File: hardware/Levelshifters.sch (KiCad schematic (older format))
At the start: 36 parts, among them U1401 SN74AXC8T245, U1402 SN74AXC8T245, U1403 SN74AXC8T245, U1404 LSF0102, U1405 LSF0102

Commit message: Length matched DDR3 Memory again.
Forgot to keep enough space between the traces and between the meander waves.

Also, I switched to Kicad 5.0 RC2.

Swaped a few ddr signals.
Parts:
- C1401, C1402, C1403, C1404, C1405, C1406, C1407, C1408: symbol C_Small -> device:C_Small
- D1401, D1402: symbol LED_Small -> device:LED_Small
- R1401, R1402, R1403, R1404, R1405, R1406, R1407, R1408, R1409, R1410, R1411, R1412, R1413, R1414, R1415, R1416, R1417, R1418, R1419, R1420, R1421: symbol R_Small -> device:R_Small
- U1401, U1402, U1403: symbol SN74AXC8T245 -> sn74axc8t245:SN74AXC8T245
- U1404, U1405: symbol LSF0102 -> lsf0102:LSF0102

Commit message: Layouted USB-UART.
Also moved USB-OTG to the right Side of the Board. To get there
some free Space, i moved the DDR3/Memory and the FPGA a few
Millimeters down.
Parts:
- R1401, R1402, R1403, R1404, R1405, R1406, R1407, R1408, R1409, R1410, R1411, R1412, R1413, R1414, R1415, R1416, R1417, R1418, R1419, R1420, R1421: footprint Resistors_SMD:R_0402 -> Resistor_SMD:R_0402_1005Metric
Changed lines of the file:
@@
 F 0 "R1407" H 3430 5820 50  0000 L CNN
 F 1 "10k" H 3430 5760 50  0000 L CNN
-F 2 "Resistors_SMD:R_0402" H 3400 5800 50  0001 C CNN
+F 2 "Resistor_SMD:R_0402_1005Metric" H 3400 5800 50  0001 C CNN
 F 3 "" H 3400 5800 50  0001 C CNN
 	1    3400 5800
@@
 F 0 "R1408" H 3430 6820 50  0000 L CNN
 F 1 "10k" H 3430 6760 50  0000 L CNN
-F 2 "Resistors_SMD:R_0402" H 3400 6800 50  0001 C CNN
+F 2 "Resistor_SMD:R_0402_1005Metric" H 3400 6800 50  0001 C CNN
 F 3 "" H 3400 6800 50  0001 C CNN
 	1    3400 6800
@@
 F 0 "R1401" H 3380 1220 50  0000 L CNN
 F 1 "10k" H 3380 1160 50  0000 L CNN
-F 2 "Resistors_SMD:R_0402" H 3350 1200 50  0001 C CNN
+F 2 "Resistor_SMD:R_0402_1005Metric" H 3350 1200 50  0001 C CNN
 F 3 "" H 3350 1200 50  0001 C CNN
 F 4 "1" H 3350 1200 60  0001 C CNN "Populated"
@@
 F 0 "R1404" H 3380 3520 50  0000 L CNN
 F 1 "10k" H 3380 3460 50  0000 L CNN
-F 2 "Resistors_SMD:R_0402" H 3350 3500 50  0001 C CNN
+F 2 "Resistor_SMD:R_0402_1005Metric" H 3350 3500 50  0001 C CNN
 F 3 "" H 3350 3500 50  0001 C CNN
 	1    3350 3500
@@
 F 0 "R1405" H 3380 4520 50  0000 L CNN
 F 1 "10k" H 3380 4460 50  0000 L CNN
-F 2 "Resistors_SMD:R_0402" H 3350 4500 50  0001 C CNN
+F 2 "Resistor_SMD:R_0402_1005Metric" H 3350 4500 50  0001 C CNN
 F 3 "" H 3350 4500 50  0001 C CNN
 	1    3350 4500
@@
 F 0 "R1403" H 3380 2420 50  0000 L CNN
 F 1 "10k" H 3380 2360 50  0000 L CNN
-F 2 "Resistors_SMD:R_0402" H 3350 2400 50  0001 C CNN
+F 2 "Resistor_SMD:R_0402_1005Metric" H 3350 2400 50  0001 C CNN
 F 3 "" H 3350 2400 50  0001 C CNN
 	1    3350 2400
@@
 F 0 "R1406" H 3380 4720 50  0000 L CNN
 F 1 "10k" H 3380 4660 50  0000 L CNN
-F 2 "Resistors_SMD:R_0402" H 3350 4700 50  0001 C CNN
+F 2 "Resistor_SMD:R_0402_1005Metric" H 3350 4700 50  0001 C CNN
 F 3 "" H 3350 4700 50  0001 C CNN
 	1    3350 4700
@@
 F 0 "R1409" H 3430 7020 50  0000 L CNN
 F 1 "10k" H 3430 6960 50  0000 L CNN
-F 2 "Resistors_SMD:R_0402" H 3400 7000 50  0001 C CNN
+F 2 "Resistor_SMD:R_0402_1005Metric" H 3400 7000 50  0001 C CNN
 F 3 "" H 3400 7000 50  0001 C CNN
 	1    3400 7000
@@
 F 0 "R1402" H 3380 2220 50  0000 L CNN
 F 1 "10k" H 3380 2160 50  0000 L CNN
-F 2 "Resistors_SMD:R_0402" H 3350 2200 50  0001 C CNN
+F 2 "Resistor_SMD:R_0402_1005Metric" H 3350 2200 50  0001 C CNN
 F 3 "" H 3350 2200 50  0001 C CNN
 	1    3350 2200
@@
 F 0 "R1417" H 9130 970 50  0000 L CNN
 F 1 "200k" H 9130 910 50  0000 L CNN
-F 2 "Resistors_SMD:R_0402" H 9100 950 50  0001 C CNN
+F 2 "Resistor_SMD:R_0402_1005Metric" H 9100 950 50  0001 C CNN
 F 3 "" H 9100 950 50  0001 C CNN
 F 4 "1" H 9100 950 60  0001 C CNN "Populated"
@@
 F 0 "R1415" H 8480 1620 50  0000 L CNN
 F 1 "300" H 8480 1560 50  0000 L CNN
-F 2 "Resistors_SMD:R_0402" H 8450 1600 50  0001 C CNN
+F 2 "Resistor_SMD:R_0402_1005Metric" H 8450 1600 50  0001 C CNN
 F 3 "" H 8450 1600 50  0001 C CNN
 F 4 "1" H 8450 1600 60  0001 C CNN "Populated"
@@
 F 0 "R1413" H 8280 1620 50  0000 L CNN
 F 1 "300" H 8280 1560 50  0000 L CNN
-F 2 "Resistors_SMD:R_0402" H 8250 1600 50  0001 C CNN
+F 2 "Resistor_SMD:R_0402_1005Metric" H 8250 1600 50  0001 C CNN
 F 3 "" H 8250 1600 50  0001 C CNN
 F 4 "1" H 8250 1600 60  0001 C CNN "Populated"
@@
 F 0 "R1419" H 10130 1320 50  0000 L CNN
 F 1 "1k" H 10130 1260 50  0000 L CNN
-F 2 "Resistors_SMD:R_0402" H 10100 1300 50  0001 C CNN
+F 2 "Resistor_SMD:R_0402_1005Metric" H 10100 1300 50  0001 C CNN
 F 3 "" H 10100 1300 50  0001 C CNN
 F 4 "1" H 10100 1300 60  0001 C CNN "Populated"
@@
 F 0 "R1421" H 10330 1320 50  0000 L CNN
 F 1 "1k" H 10330 1260 50  0000 L CNN
-F 2 "Resistors_SMD:R_0402" H 10300 1300 50  0001 C CNN
+F 2 "Resistor_SMD:R_0402_1005Metric" H 10300 1300 50  0001 C CNN
 F 3 "" H 10300 1300 50  0001 C CNN
 F 4 "1" H 10300 1300 60  0001 C CNN "Populated"
@@
 F 0 "R1416" H 9080 3420 50  0000 L CNN
 F 1 "200k" H 9080 3360 50  0000 L CNN
-F 2 "Resistors_SMD:R_0402" H 9050 3400 50  0001 C CNN
+F 2 "Resistor_SMD:R_0402_1005Metric" H 9050 3400 50  0001 C CNN
 F 3 "" H 9050 3400 50  0001 C CNN
 F 4 "1" H 9050 3400 60  0001 C CNN "Populated"
@@
 F 0 "R1414" H 8430 4070 50  0000 L CNN
 F 1 "300" H 8430 4010 50  0000 L CNN
-F 2 "Resistors_SMD:R_0402" H 8400 4050 50  0001 C CNN
+F 2 "Resistor_SMD:R_0402_1005Metric" H 8400 4050 50  0001 C CNN
 F 3 "" H 8400 4050 50  0001 C CNN
 F 4 "1" H 8400 4050 60  0001 C CNN "Populated"
@@
 F 0 "R1412" H 8230 4070 50  0000 L CNN
 F 1 "300" H 8230 4010 50  0000 L CNN
-F 2 "Resistors_SMD:R_0402" H 8200 4050 50  0001 C CNN
+F 2 "Resistor_SMD:R_0402_1005Metric" H 8200 4050 50  0001 C CNN
 F 3 "" H 8200 4050 50  0001 C CNN
 F 4 "1" H 8200 4050 60  0001 C CNN "Populated"
@@
 F 0 "R1418" H 10080 3770 50  0000 L CNN
 F 1 "1k" H 10080 3710 50  0000 L CNN
-F 2 "Resistors_SMD:R_0402" H 10050 3750 50  0001 C CNN
+F 2 "Resistor_SMD:R_0402_1005Metric" H 10050 3750 50  0001 C CNN
 F 3 "" H 10050 3750 50  0001 C CNN
 F 4 "1" H 10050 3750 60  0001 C CNN "Populated"
@@
 F 0 "R1420" H 10280 3770 50  0000 L CNN
 F 1 "1k" H 10280 3710 50  0000 L CNN
-F 2 "Resistors_SMD:R_0402" H 10250 3750 50  0001 C CNN
+F 2 "Resistor_SMD:R_0402_1005Metric" H 10250 3750 50  0001 C CNN
 F 3 "" H 10250 3750 50  0001 C CNN
 F 4 "1" H 10250 3750 60  0001 C CNN "Populated"
@@
 F 0 "R1410" V 4800 4300 50  0000 L CNN
 F 1 "420" V 4700 3950 50  0000 L CNN
-F 2 "Resistors_SMD:R_0402" H 4750 4200 50  0001 C CNN
+F 2 "Resistor_SMD:R_0402_1005Metric" H 4750 4200 50  0001 C CNN
 F 3 "" H 4750 4200 50  0001 C CNN
 F 4 "1" H 4750 4200 60  0001 C CNN "Populated"
@@
 F 0 "R1411" V 4800 4400 50  0000 L CNN
 F 1 "420" V 4700 4050 50  0000 L CNN
-F 2 "Resistors_SMD:R_0402" H 4750 4300 50  0001 C CNN
+F 2 "Resistor_SMD:R_0402_1005Metric" H 4750 4300 50  0001 C CNN
 F 3 "" H 4750 4300 50  0001 C CNN
 F 4 "1" H 4750 4300 60  0001 C CNN "Populated"

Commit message: Improved Powerdistribution Network of the FPGA.
Also started to layout USB.
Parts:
- C1401, C1402, C1403, C1404, C1405, C1406, C1407, C1408: footprint Capacitors_SMD:C_0201 -> Capacitor_SMD:C_0201_0603Metric
- U1401: footprint footprints:VQFN-24 -> footprints:TI_RHL_R-PVQFN-N24_3.5x5.5mm_0.5mm-pitch
- U1402, U1403: footprint footprints:VQFN-24 -> footprints:TI_RHL_R-PVQFN-N24_3.5x5.5mm_0.5mm-pitch; Populate for CLG484(Z-7012s/Z-7015) (none) -> 1; Populate for SBGA485(Z-7030) (none) -> 1
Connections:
- wire segments 163 -> 183

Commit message: Fixed Schematic Symbols
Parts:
- C1401, C1402, C1403, C1404, C1405, C1406, C1407, C1408: symbol device:C_Small -> Device:C_Small
- D1401, D1402: symbol device:LED_Small -> Device:LED_Small
- R1401, R1402, R1403, R1404, R1405, R1406, R1407, R1408, R1409, R1410, R1411, R1412, R1413, R1414, R1415, R1416, R1417, R1418, R1419, R1420, R1421: symbol device:R_Small -> Device:R_Small
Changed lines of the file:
@@
 $Descr A4 11693 8268
 encoding utf-8
-Sheet 14 22
+Sheet 14 21
 Title ""
 Date ""
@@
 $EndComp
 $Comp
-L power1:+1V8 #PWR0153
+L power:+1V8 #PWR0153
 U 1 1 5ADF1CB7
 P 3500 5500
@@
 $EndComp
 $Comp
-L power1:+3.3V #PWR0154
+L power:+3V3 #PWR0154
 U 1 1 5ADF1CEC
 P 4700 5500
@@
 $EndComp
 $Comp
-L device:R_Small R1407
+L Device:R_Small R1407
 U 1 1 5ADF2FCD
 P 3400 5800
@@
 $EndComp
 $Comp
-L device:R_Small R1408
+L Device:R_Small R1408
 U 1 1 5ADF30A0
 P 3400 6800
@@
 $EndComp
 $Comp
-L power1:GND #PWR0155
+L power:GND #PWR0155
 U 1 1 5ADF5482
 P 3450 2650
@@
 $EndComp
 $Comp
-L power1:+1V8 #PWR0156
+L power:+1V8 #PWR0156
 U 1 1 5ADF5488
 P 3450 900
@@
 $EndComp
 $Comp
-L power1:+3.3V #PWR0157
+L power:+3V3 #PWR0157
 U 1 1 5ADF5492
 P 4650 900
@@
 $EndComp
 $Comp
-L device:R_Small R1401
+L Device:R_Small R1401
 U 1 1 5ADF54A5
 P 3350 1200
@@
 $EndComp
 $Comp
-L power1:+1V8 #PWR0158
+L power:+1V8 #PWR0158
 U 1 1 5ADF5FE1
 P 3450 3200
@@
 $EndComp
 $Comp
-L power1:+3.3V #PWR0159
+L power:+3V3 #PWR0159
 U 1 1 5ADF5FE7
 P 4650 3200
@@
 $EndComp
 $Comp
-L device:R_Small R1404
+L Device:R_Small R1404
 U 1 1 5ADF5FED
 P 3350 3500
@@
 $EndComp
 $Comp
-L device:R_Small R1405
+L Device:R_Small R1405
 U 1 1 5ADF5FF9
 P 3350 4500
@@
 If needed while routing, these level shifters can be rotated
 $Comp
-L power1:+1V8 #PWR0160
+L power:+1V8 #PWR0160
 U 1 1 5AE0B26C
 P 8900 700
@@
 $EndComp
 $Comp
-L power1:+3.3V #PWR0161
+L power:+3V3 #PWR0161
 U 1 1 5AE0B286
 P 9100 700
@@
 $EndComp
 $Comp
-L device:C_Small C1401
+L Device:C_Small C1401
 U 1 1 5AE0CA09
 P 650 4150
@@
 $EndComp
 $Comp
-L device:C_Small C1402
+L Device:C_Small C1402
 U 1 1 5AE0CAE1
 P 950 4150
@@
 $EndComp
 $Comp
-L device:C_Small C1403
+L Device:C_Small C1403
 U 1 1 5AE0CB91
 P 1250 4150
@@
 $EndComp
 $Comp
-L power1:GND #PWR0162
+L power:GND #PWR0162
 U 1 1 5AE0CE71
 P 950 4450
@@
 $EndComp
 $Comp
-L power1:+1V8 #PWR0163
+L power:+1V8 #PWR0163
 U 1 1 5AE0CF5D
 P 950 3850
@@
 $EndComp
 $Comp
-L device:C_Small C1404
+L Device:C_Small C1404
 U 1 1 5AE0D175
 P 1600 4150
@@
 $EndComp
 $Comp
-L device:C_Small C1405
+L Device:C_Small C1405
 U 1 1 5AE0D17B
 P 1900 4150
@@
 $EndComp
 $Comp
-L device:C_Small C1406
+L Device:C_Small C1406
 U 1 1 5AE0D181
 P 2200 4150
@@
 $EndComp
 $Comp
-L power1:GND #PWR0164
+L power:GND #PWR0164
 U 1 1 5AE0D191
 P 1900 4450
@@
 $EndComp
 $Comp
-L power1:+3.3V #PWR0165
+L power:+3V3 #PWR0165
 U 1 1 5AE0D1EF
 P 1900 3850
@@
 Bypass Capacitors for the levelshifters.\nPlace near their Powerinputs
 $Comp
-L power1:GND #PWR0166
+L power:GND #PWR0166
 U 1 1 5AE25E02
 P 3450 4950
@@
 $EndComp
 $Comp
-L power1:GND #PWR0167
+L power:GND #PWR0167
 U 1 1 5AE25E5E
 P 3500 7250
@@
 $EndComp
 $Comp
-L power1:GND #PWR0168
+L power:GND #PWR0168
 U 1 1 5AE28D57
 P 3200 5800
@@
 $EndComp
 $Comp
-L power1:+1V8 #PWR0169
+L power:+1V8 #PWR0169
 U 1 1 5AE28DB3
 P 3200 6800
@@
 SFP_SDA_18
 $Comp
-L power1:GND #PWR0170
+L power:GND #PWR0170
 U 1 1 5ADF54AB
 P 3150 4500
@@
 $EndComp
 $Comp
-L power1:+1V8 #PWR0171
+L power:+1V8 #PWR0171
 U 1 1 5AE2AC7B
 P 3150 3500
@@
 $EndComp
 $Comp
-L power1:+1V8 #PWR0172
+L power:+1V8 #PWR0172
 U 1 1 5AE2ACD7
 P 3150 1200
@@
 CAM_SPI_MISO_18
 $Comp
-L device:R_Small R1403
+L Device:R_Small R1403
 U 1 1 5AE2CB0B
 P 3350 2400
@@
 $EndComp
 $Comp
-L power1:GND #PWR0173
+L power:GND #PWR0173
 U 1 1 5AE2CB13
 P 3150 2400
@@
 $EndComp
 $Comp
-L device:R_Small R1406
+L Device:R_Small R1406
 U 1 1 5AE2CBEF
 P 3350 4700
@@
 $EndComp
 $Comp
-L power1:GND #PWR0174
+L power:GND #PWR0174
 U 1 1 5AE2CBF7
 P 3150 4700
@@
 $EndComp
 $Comp
-L device:R_Small R1409
+L Device:R_Small R1409
 U 1 1 5AE2CDAE
 P 3400 7000
@@
 $EndComp
 $Comp
-L power1:GND #PWR0175
+L power:GND #PWR0175
 U 1 1 5AE2CDB6
 P 3200 7000
@@
 DIR[1:2] = 10\nA[1:4] => B[1:4]; A[5:8] => B[5:8]
 $Comp
-L device:R_Small R1402
+L Device:R_Small R1402
 U 1 1 5AE6E608
 P 3350 2200
@@
 $EndComp
 $Comp
-L power1:GND #PWR0176
+L power:GND #PWR0176
 U 1 1 5AE6E60E
 P 3150 2200
@@
 	8900 700  8900 1050
 $Comp
-L power1:GND #PWR0177
+L power:GND #PWR0177
 U 1 1 5AF1DBA2
 P 9000 2650
@@
 	9500 1900 10100 1900
 $Comp
-L device:R_Small R1417
+L Device:R_Small R1417
 U 1 1 5AF233F3
 P 9100 950
@@
 Connection ~ 9100 1100
 $Comp
-L device:C_Small C1408
+L Device:C_Small C1408
 U 1 1 5AF23DA1
 P 9900 1300
@@
 $EndComp
 $Comp
-L power1:GND #PWR0178
+L power:GND #PWR0178
 U 1 1 5AF23FED
 P 9900 1500
@@
 	9900 1500 9900 1400
 $Comp
-L device:R_Small R1415
+L Device:R_Small R1415
 U 1 1 5AF2618E
 P 8450 1600
@@
 $EndComp
 $Comp
-L device:R_Small R1413
+L Device:R_Small R1413
 U 1 1 5AF262AE
 P 8250 1600
@@
 Connection ~ 9600 1100
 $Comp
-L device:R_Small R1419
+L Device:R_Small R1419
 U 1 1 5AF27A1B
 P 10100 1300
@@
 $EndComp
 $Comp
-L device:R_Small R1421
+L Device:R_Small R1421
 U 1 1 5AF27C23
 P 10300 1300
@@
 Connection ~ 10100 750
 $Comp
-L power1:+1V8 #PWR0179
+L power:+1V8 #PWR0179
 U 1 1 5AF2950E
 P 8850 3150
@@
 $EndComp
 $Comp
-L power1:+3.3V #PWR0180
+L power:+3V3 #PWR0180
 U 1 1 5AF29514
 P 9050 3150
@@
 	8850 3150 8850 3500
 $Comp
-L power1:GND #PWR0181
+L power:GND #PWR0181
 U 1 1 5AF2952A
 P 8950 5100
@@
 	9450 4350 10050 4350
 $Comp
-L device:R_Small R1416
+L Device:R_Small R1416
 U 1 1 5AF2953D
 P 9050 3400
@@
 Connection ~ 9050 3550
 $Comp
-L device:C_Small C1407
+L Device:C_Small C1407
 U 1 1 5AF29550
 P 9850 3750
@@
 $EndComp
 $Comp
-L power1:GND #PWR0182
+L power:GND #PWR0182
 U 1 1 5AF29556
 P 9850 3950
@@
 	9850 3950 9850 3850
 $Comp
-L device:R_Small R1414
+L Device:R_Small R1414
 U 1 1 5AF29561
 P 8400 4050
@@
 $EndComp
 $Comp
-L device:R_Small R1412
+L Device:R_Small R1412
 U 1 1 5AF2956B
 P 8200 4050
@@
 Connection ~ 9550 3550
 $Comp
-L device:R_Small R1418
+L Device:R_Small R1418
 U 1 1 5AF29581
 P 10050 3750
@@
 $EndComp
 $Comp
-L device:R_Small R1420
+L Device:R_Small R1420
 U 1 1 5AF2958B
 P 10250 3750
@@
 	3550 4300 3250 4300
 $Comp
-L device:LED_Small D1401
+L Device:LED_Small D1401
 U 1 1 5AF4B3E8
 P 5050 4200
@@
 $EndComp
 $Comp
-L device:R_Small R1410
+L Device:R_Small R1410
 U 1 1 5AF4B4AF
 P 4750 4200
@@
 	4850 4200 4950 4200
 $Comp
-L device:LED_Small D1402
+L Device:LED_Small D1402
 U 1 1 5AF4B957
 P 5050 4300
@@
 $EndComp
 $Comp
-L device:R_Small R1411
+L Device:R_Small R1411
 U 1 1 5AF4B961
 P 4750 4300
@@
 	4850 4300 4950 4300
 $Comp
-L power1:GND #PWR0183
+L power:GND #PWR0183
 U 1 1 5AF4C0A5
 P 5350 4250

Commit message: WIP: TLK Powerdistribution
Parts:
- removed D1401, D1402: LED_Small, LEDs:LED_0402, symbol Device:LED_Small
- added D1301, D1302: LED_ALT, LED_SMD:LED_0603_1608Metric, symbol Device:LED_ALT
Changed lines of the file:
@@
 EESchema Schematic File Version 4
-LIBS:zynq_board-cache
 EELAYER 26 0
 EELAYER END
 $Descr A4 11693 8268
 encoding utf-8
-Sheet 14 21
+Sheet 13 21
 Title ""
 Date ""
@@
 	3550 4300 3250 4300
 $Comp
-L Device:LED_Small D1401
-U 1 1 5AF4B3E8
-P 5050 4200
-F 0 "D1401" H 4950 4150 50  0000 L CNN
-F 1 "LED_Small" H 4900 4050 50  0000 L CNN
-F 2 "LEDs:LED_0402" V 5050 4200 50  0001 C CNN
-F 3 "" V 5050 4200 50  0001 C CNN
-F 4 "1" H 5050 4200 60  0001 C CNN "Populated"
-F 5 "SPEC" H 5050 4200 60  0001 C CNN "Source"
-F 6 "1" H 5050 4200 60  0001 C CNN "Populate for SBGA485(Z-7030)"
-F 7 "1" H 5050 4200 60  0001 C CNN "Populate for CLG484(Z-7012s/Z-7015)"
-	1    5050 4200
-	-1   0    0    1
-$EndComp
-$Comp
 L Device:R_Small R1410
 U 1 1 5AF4B4AF
@@
 Wire Wire Line
 	4650 4200 4550 4200
-Wire Wire Line
-	4850 4200 4950 4200
-$Comp
-L Device:LED_Small D1402
-U 1 1 5AF4B957
-P 5050 4300
-F 0 "D1402" H 4950 4400 50  0000 L CNN
-F 1 "LED_Small" H 4850 4500 50  0000 L CNN
-F 2 "LEDs:LED_0402" V 5050 4300 50  0001 C CNN
-F 3 "" V 5050 4300 50  0001 C CNN
-F 4 "1" H 5050 4300 60  0001 C CNN "Populated"
-F 5 "SPEC" H 5050 4300 60  0001 C CNN "Source"
-F 6 "1" H 5050 4300 60  0001 C CNN "Populate for SBGA485(Z-7030)"
-F 7 "1" H 5050 4300 60  0001 C CNN "Populate for CLG484(Z-7012s/Z-7015)"
-	1    5050 4300
-	-1   0    0    1
-$EndComp
 $Comp
 L Device:R_Small R1411
@@
 Wire Wire Line
 	4650 4300 4550 4300
-Wire Wire Line
-	4850 4300 4950 4300
 $Comp
 L power:GND #PWR0183
@@
 $EndComp
 Wire Wire Line
-	5150 4200 5250 4200
-Wire Wire Line
 	5250 4200 5250 4250
-Wire Wire Line
-	5250 4300 5150 4300
 Wire Wire Line
 	5350 4250 5250 4250
@@
 Wire Wire Line
 	3500 7150 3500 7250
+$Comp
+L Device:LED_ALT D1301
+U 1 1 5B315043
+P 5050 4200
+F 0 "D1301" H 5041 4416 50  0000 C CNN
+F 1 "LED_ALT" H 5041 4325 50  0000 C CNN
+F 2 "LED_SMD:LED_0603_1608Metric" H 5050 4200 50  0001 C CNN
+F 3 "http://www.qt-brightek.com/datasheet/QBLP617_series.pdf" H 5050 4200 50  0001 C CNN
+F 4 "QT Brightek (QTB)" H 5050 4200 50  0001 C CNN "MFG Name"
+F 5 "QBLP617-R" H 5050 4200 50  0001 C CNN "MFG Part Num"
+F 6 "1516-1081-1-ND" H 5050 4200 50  0001 C CNN "Digikey"
+F 7 "1" H 5050 4200 50  0001 C CNN "Populated"
+F 8 "LED RED CLEAR 2SMD R/A" H 5050 4200 50  0001 C CNN "Description"
+F 9 "SPEC" H 5050 4200 50  0001 C CNN "Source"
+F 10 "1" H 5050 4200 50  0001 C CNN "Populate for SBGA485(Z-7030)"
+F 11 "1" H 5050 4200 50  0001 C CNN "Populate for CLG484(Z-7012s/Z-7015)"
+	1    5050 4200
+	-1   0    0    1
+$EndComp
+Wire Wire Line
+	4850 4200 4900 4200
+Wire Wire Line
+	5200 4200 5250 4200
+$Comp
+L Device:LED_ALT D1302
+U 1 1 5B32E92E
+P 5050 4300
+F 0 "D1302" H 5041 4516 50  0000 C CNN
+F 1 "LED_ALT" H 5041 4425 50  0000 C CNN
+F 2 "LED_SMD:LED_0603_1608Metric" H 5050 4300 50  0001 C CNN
+F 3 "http://www.qt-brightek.com/datasheet/QBLP617_series.pdf" H 5050 4300 50  0001 C CNN
+F 4 "QT Brightek (QTB)" H 5050 4300 50  0001 C CNN "MFG Name"
+F 5 "QBLP617-R" H 5050 4300 50  0001 C CNN "MFG Part Num"
+F 6 "1516-1081-1-ND" H 5050 4300 50  0001 C CNN "Digikey"
+F 7 "1" H 5050 4300 50  0001 C CNN "Populated"
+F 8 "LED RED CLEAR 2SMD R/A" H 5050 4300 50  0001 C CNN "Description"
+F 9 "SPEC" H 5050 4300 50  0001 C CNN "Source"
+F 10 "1" H 5050 4300 50  0001 C CNN "Populate for SBGA485(Z-7030)"
+F 11 "1" H 5050 4300 50  0001 C CNN "Populate for CLG484(Z-7012s/Z-7015)"
+	1    5050 4300
+	-1   0    0    1
+$EndComp
+Wire Wire Line
+	5200 4300 5250 4300
+Wire Wire Line
+	4900 4300 4850 4300
 $EndSCHEMATC

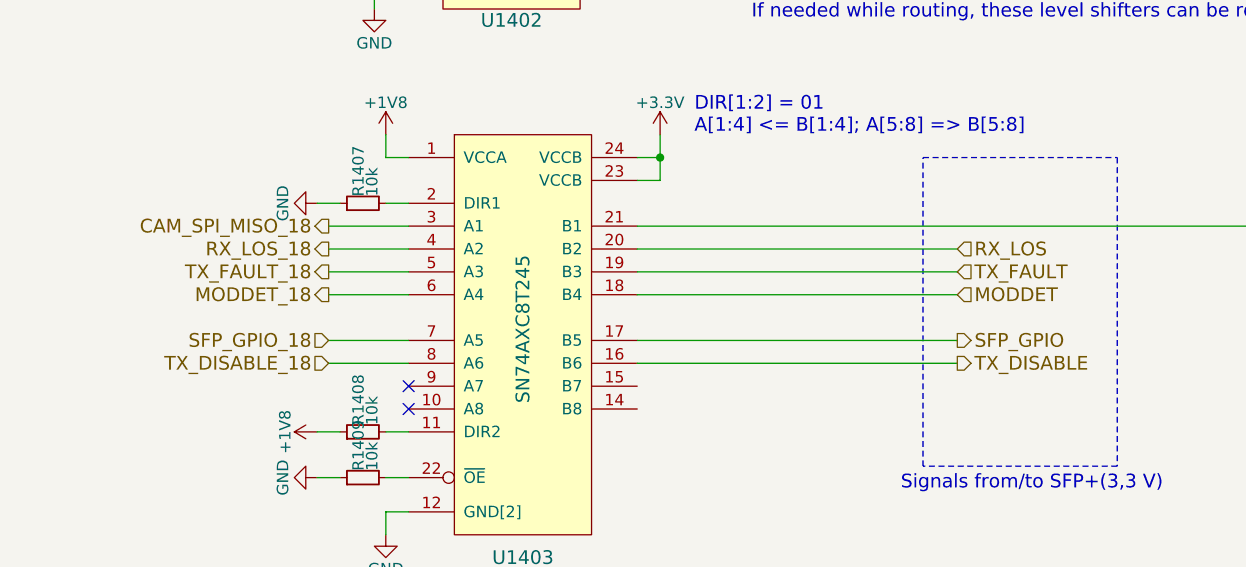
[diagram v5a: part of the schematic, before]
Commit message: SFP+ Power Filter, Levelshifter and MGT/TLK Clock Distribution.
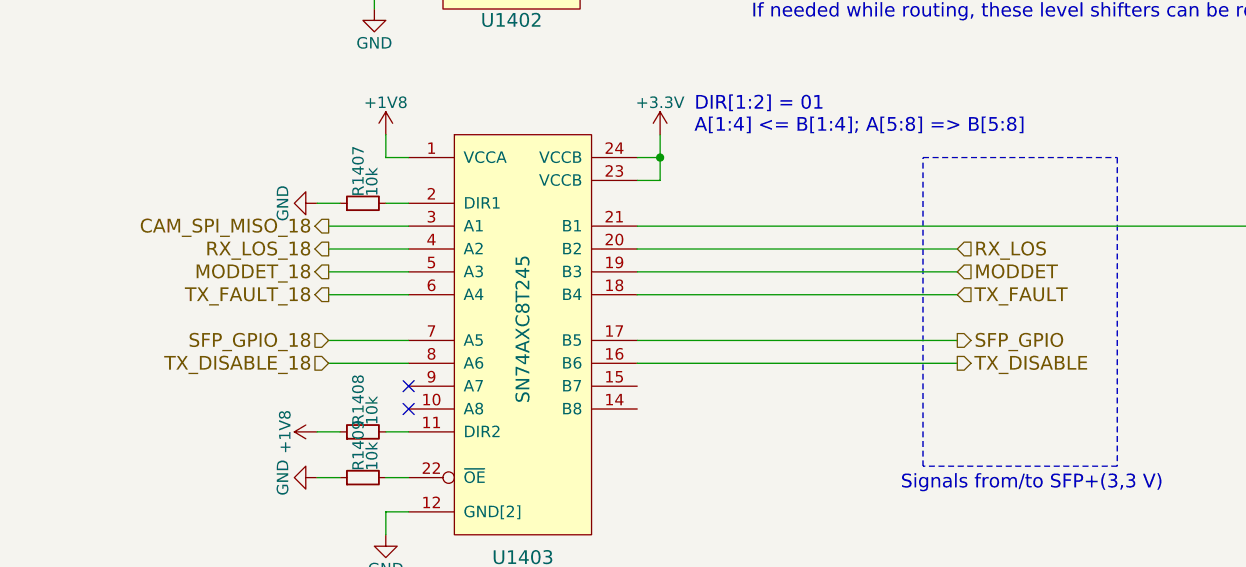
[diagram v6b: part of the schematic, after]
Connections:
- net MODDET: now also U1403.19 (B3); no longer U1403.18 (B4)
- net MODDET_18: now also U1403.5 (A3); no longer U1403.6 (A4)
- net TX_FAULT: now also U1403.18 (B4); no longer U1403.19 (B3)
- net TX_FAULT_18: now also U1403.6 (A4); no longer U1403.5 (A3)
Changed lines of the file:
@@
 Text HLabel 6000 6500 2    60   Output ~ 0
 TX_DISABLE
-Text HLabel 6000 6100 2    60   Input ~ 0
+Text HLabel 6000 6200 2    60   Input ~ 0
 TX_FAULT
 Text HLabel 10550 4350 2    60   BiDi ~ 0
@@
 Text HLabel 10550 4250 2    60   BiDi ~ 0
 SFP_SCL
-Text HLabel 6000 6200 2    60   Input ~ 0
+Text HLabel 6000 6100 2    60   Input ~ 0
 MODDET
 Text HLabel 6000 6000 2    60   Input ~ 0
@@
 Text HLabel 3250 6000 0    60   Output ~ 0
 RX_LOS_18
+Text HLabel 3250 6200 0    60   Output ~ 0
+TX_FAULT_18
 Text HLabel 3250 6100 0    60   Output ~ 0
-TX_FAULT_18
-Text HLabel 3250 6200 0    60   Output ~ 0
 MODDET_18
 Text HLabel 3250 6400 0    60   Input ~ 0
